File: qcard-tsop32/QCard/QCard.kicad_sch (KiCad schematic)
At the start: 3 parts, among them J1 Conn_02x18_Top_Bottom, U1 SST39SF040

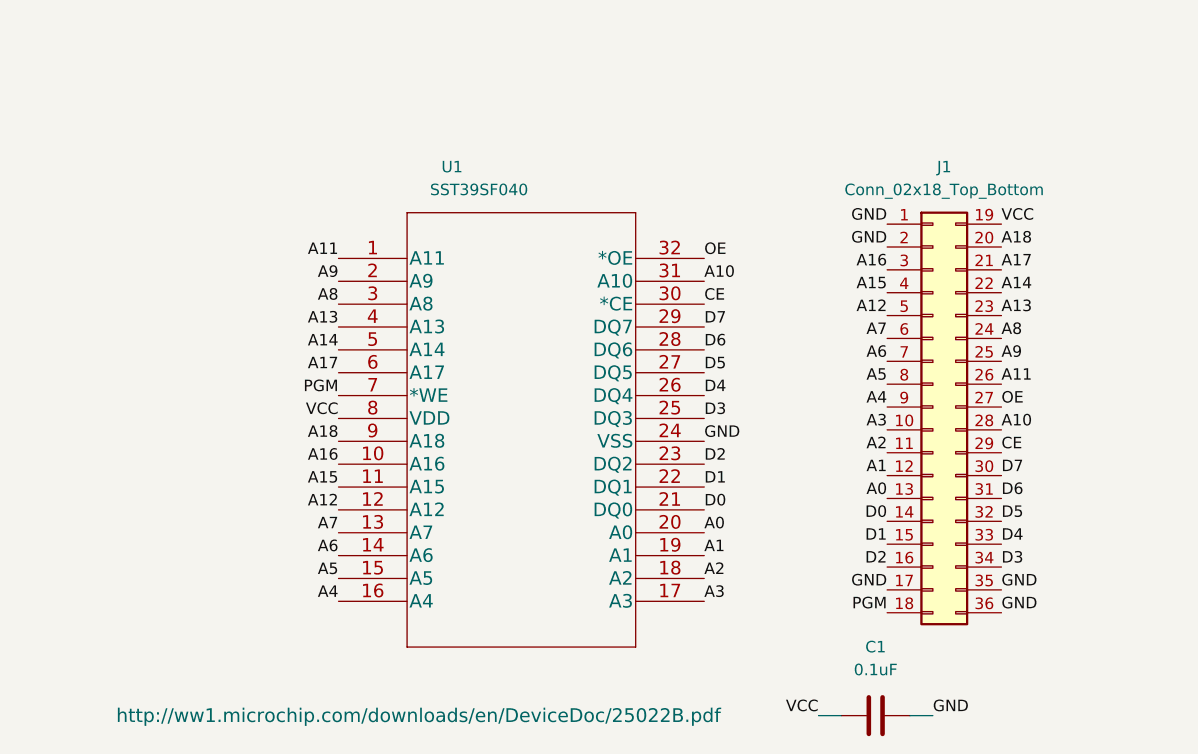
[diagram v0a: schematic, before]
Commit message: Adds jumper for programming, fixes all DRC errors but loses mounting holes
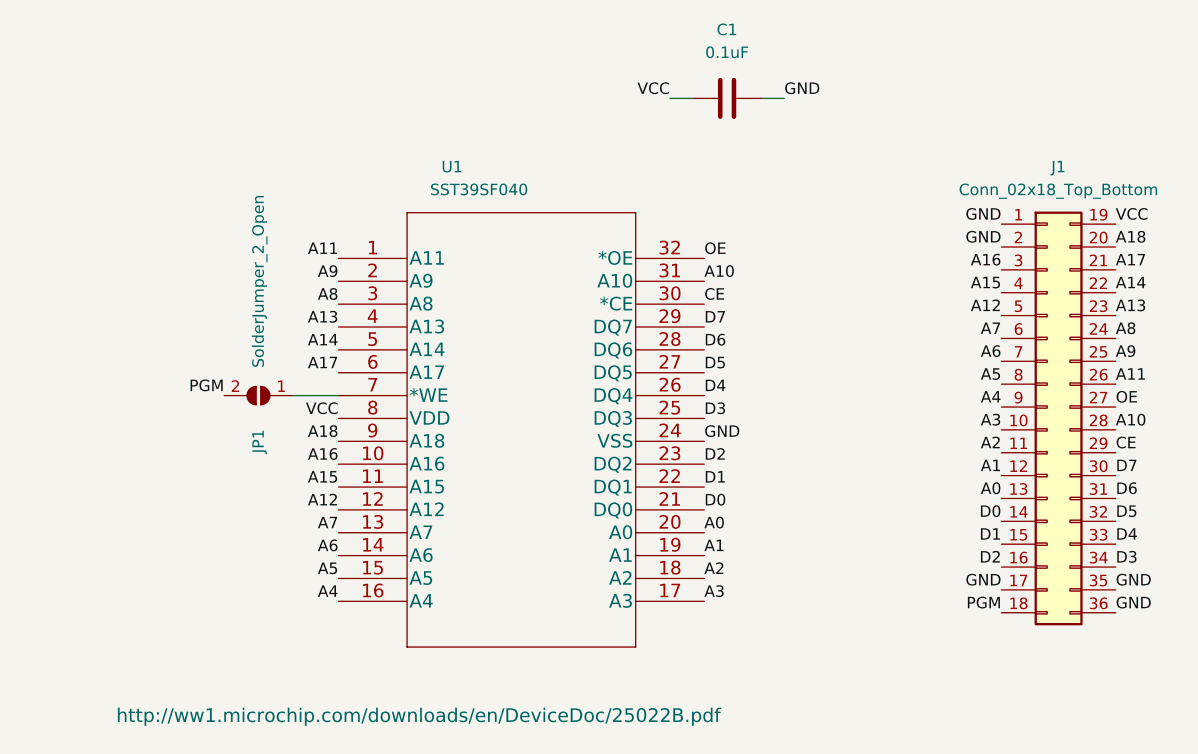
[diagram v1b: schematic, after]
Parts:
- added JP1: SolderJumper_2_Open, Jumper:SolderJumper-2_P1.3mm_Open_RoundedPad1.0x1.5mm, symbol Jumper:SolderJumper_2_Open
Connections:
- net PGM: now also JP1.2 (B); no longer U1.7 (*WE)
- new net: JP1.1 (A), U1.7 (*WE)
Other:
- moved on the sheet: C1, J1
